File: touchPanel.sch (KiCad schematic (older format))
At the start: 54 parts, among them J19 Mono_AudioConnector, J20 Mono_AudioConnector, J21 Mono_AudioConnector, J22 Mono_AudioConnector

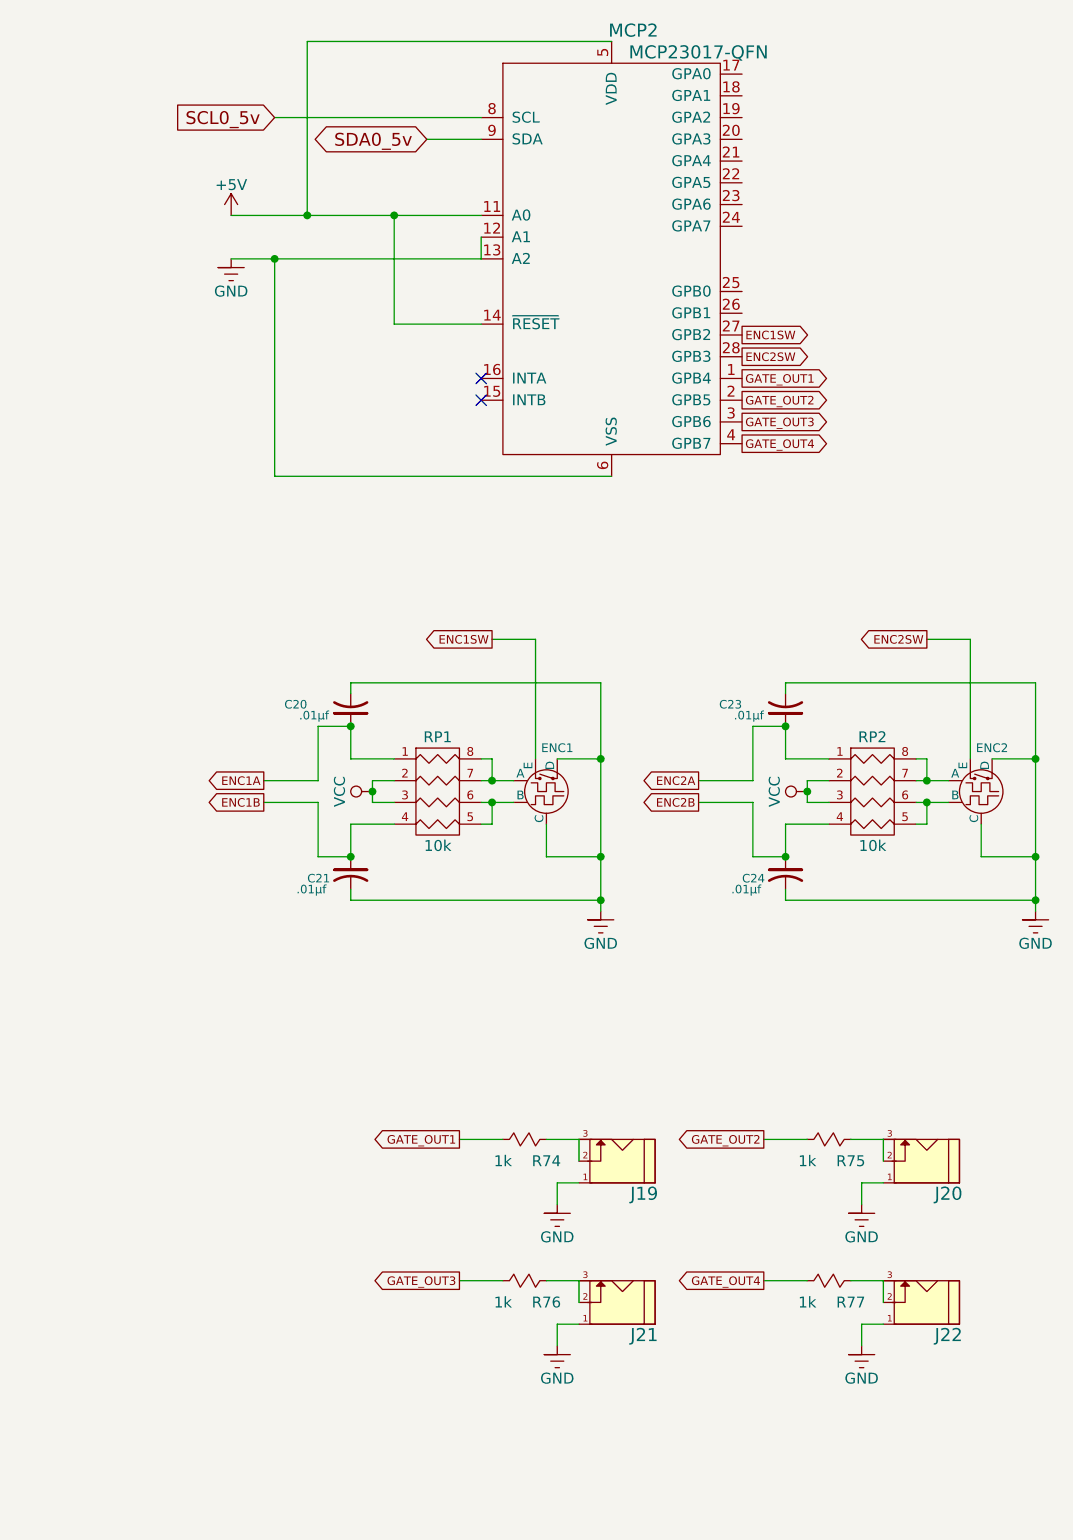
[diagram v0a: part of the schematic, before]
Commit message: Added Touch Capacitive Panel
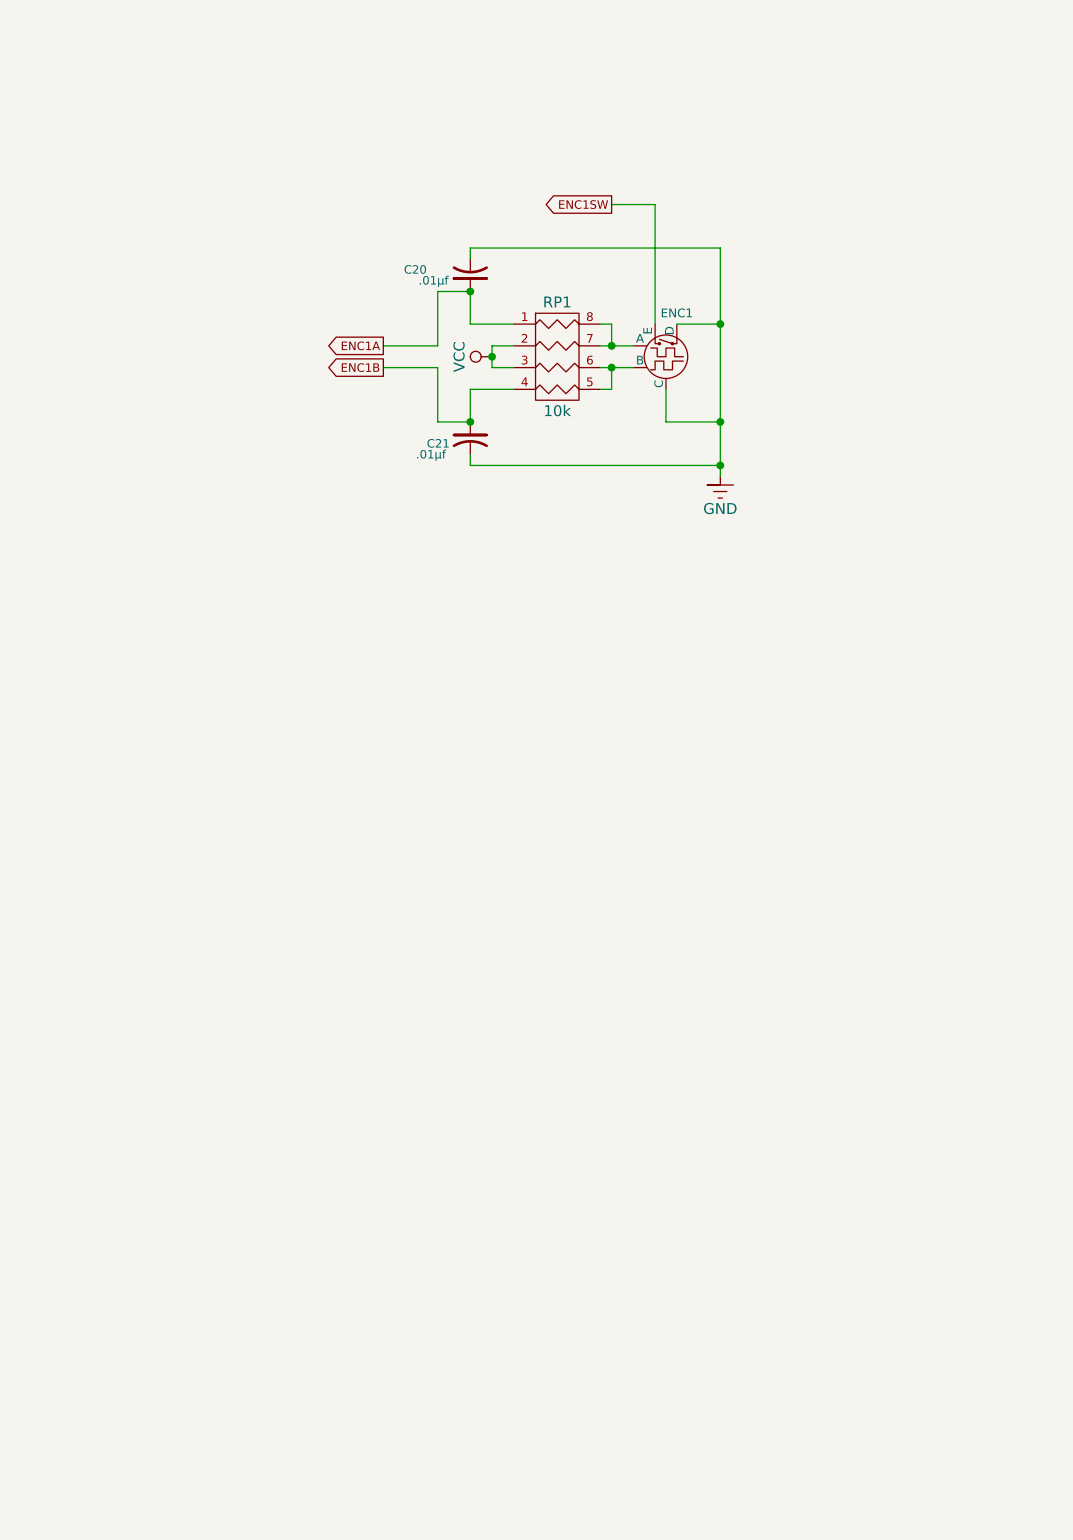
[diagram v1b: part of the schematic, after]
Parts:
- removed C23, C24: .01µf, Capacitors_SMD:C_0805_HandSoldering, symbol Cap
- removed ENC2: Encoder_switch, Zetaohm:AB2_ROTARY_ENCODER_W_SWITCH, symbol Encoder_switch
- removed J19, J20, J21, J22: Mono_AudioConnector, Zetaohm:THONKICONN, symbol Mono_AudioConnector
- removed MCP2: MCP23017-QFN, Housings_DFN_QFN:QFN-28-1EP_6x6mm_Pitch0.65mm, symbol MCP23017-QFN
- removed R74, R75, R76, R77: 1k, Resistors_SMD:R_0805_HandSoldering, symbol Resistor
- removed RP2: 10k, symbol R_PACK4
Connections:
- no-connect marks 2 -> 0
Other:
- moved on the sheet: C20, C21, ENC1, RP1

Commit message: Updating footprints
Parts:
- C20, C21: footprint Capacitors_SMD:C_0805_HandSoldering -> Capacitors_SMD:C_0603_HandSoldering
- C36, C41, C42, C43, C44, C45, C46, C47, C48, C49, C50, C51, C52: renamed from C?; footprint (none) -> Capacitors_SMD:C_0603_HandSoldering
- R15, R47, R48, R49, R50, R74, R75, R76, R77, R78, R79, R80, R81, R82, R83, R84, R85, R86, R87, R88: renamed from R?; footprint (none) -> Resistors_SMD:R_0603_HandSoldering
- RP1: footprint (none) -> Resistors_SMD:R_0603_HandSoldering
- U11: renamed from U?; footprint (none) -> Housings_SOT-23_SOT-143_TSOT-6:SOT-23_Handsoldering
- U12: renamed from U?; footprint (none) -> Housings_QFP:LQFP-44_10x10mm_Pitch0.8mm
- gave numbers to parts that had none: 2
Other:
- moved on the sheet: U14

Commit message: Populating pcb file
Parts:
- removed R48, R49, R50, R74, R75, R76, R77, R78, R79, R80, R81, R82: 1k, Resistors_SMD:R_0603_HandSoldering, symbol Resistor
- removed R85, R86, R87, R88: 470k, Resistors_SMD:R_0603_HandSoldering, symbol Resistor
- added RP2, RP3, RP4: 1k, Resistors_SMD:R_Array_Convex_4x0603, symbol R_PACK4
- added RP5: 470k, Resistors_SMD:R_Array_Convex_4x0603, symbol R_PACK4
- RP1: footprint Resistors_SMD:R_0603_HandSoldering -> Resistors_SMD:R_Array_Convex_4x0603
- U14: footprint (none) -> Zetaohm:FACEPLATEV1
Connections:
- net X0: now also RP2.8 (R1); no longer R15.1
- net X1: now also RP2.7 (R2); no longer R47.1
- net X2: now also RP2.6 (R3)
- net X3: now also RP2.5 (R4)
- net X4: now also RP3.8 (R1)
- net X5: now also RP3.7 (R2)
- net X6: now also RP3.6 (R3)
- net X7: now also RP3.5 (R4)
- net Y0: now also RP4.8 (R1)
- net Y1: now also RP4.7 (R2)
- net Y2: now also RP4.6 (R3)
- net Y3: now also RP4.5 (R4)
- net Y4: now also R15.1
- net Y5: now also R47.1
- net at R83.1, R84.1, U12.12 (SMP): now also RP5.5 (R4), RP5.6 (R3), RP5.7 (R2), RP5.8 (R1)
- net at C50.1, U12.13 (Y3A): now also RP4.4 (P4)
- net at C49.1, U12.14 (Y2A): now also RP4.3 (P3)
- net at C47.1, U12.15 (Y1A): now also RP4.2 (P2)
- net at C45.1, U12.16 (Y0A): now also RP4.1 (P1)
- net at U12.19 (X0): now also RP2.1 (P1); no longer R15.2
- net at U12.20 (X1): now also RP2.2 (P2); no longer R47.2
- net at U12.21 (X2): now also RP2.3 (P3)
- net at U12.22 (X3): now also RP2.4 (P4)
- net at U12.23 (X4): now also RP3.1 (P1)
- net at U12.24 (X5): now also RP3.2 (P2)
- net at U12.25 (X6): now also RP3.3 (P3)
- net at U12.26 (X7): now also RP3.4 (P4)
- net at C45.2, U12.30 (Y0B): now also RP5.1 (P1)
- net at C47.2, U12.31 (Y1B): now also RP5.2 (P2)
- net at C49.2, U12.32 (Y2B): now also RP5.3 (P3)
- net at C50.2, U12.33 (Y3B): now also RP5.4 (P4)
- net at C51.1, U12.34 (Y4A): now also R15.2
- net at U12.36 (Y5A): now also R47.2
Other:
- moved on the sheet: R83, R84

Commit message: UPDATING SCHEMATIC FOR SSD1327
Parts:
- U14: footprint Zetaohm:FACEPLATEV1 -> Zetaohm:AFX-01_FACEPLATE
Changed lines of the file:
@@
 $Descr User 15748 9843
 encoding utf-8
-Sheet 6 7
+Sheet 6 8
 Title ""
 Date ""
@@
 $EndComp
 $Comp
-L GND-RESCUE-afx-01 #PWR96
+L GND-RESCUE-afx-01 #PWR092
 U 1 1 56243B05
 P 13350 3150
-F 0 "#PWR96" H 13350 2900 50  0001 C CNN
+F 0 "#PWR092" H 13350 2900 50  0001 C CNN
 F 1 "GND" H 13350 3000 50  0000 C CNN
 F 2 "" H 13350 3150 60  0000 C CNN
@@
 $EndComp
 $Comp
-L VCC #PWR95
+L VCC #PWR093
 U 1 1 56243B1B
 P 12300 2600
-F 0 "#PWR95" H 12300 2450 50  0001 C CNN
+F 0 "#PWR093" H 12300 2450 50  0001 C CNN
 F 1 "VCC" H 12300 2750 50  0000 C CNN
 F 2 "" H 12300 2600 60  0000 C CNN
@@
 $EndComp
 $Comp
-L +5V #PWR92
+L +5V #PWR094
 U 1 1 56248DD8
 P 1950 1500
-F 0 "#PWR92" H 1950 1350 50  0001 C CNN
+F 0 "#PWR094" H 1950 1350 50  0001 C CNN
 F 1 "+5V" H 1950 1640 50  0000 C CNN
 F 2 "" H 1950 1500 60  0000 C CNN
@@
 F 0 "U14" H 12150 4200 60  0000 C CNN
 F 1 "AFX-01_BUTTON_MATRIX" H 12150 5200 60  0000 C CNN
-F 2 "Zetaohm:FACEPLATEV1" H 12150 4650 60  0001 C CNN
+F 2 "Zetaohm:AFX-01_FACEPLATE" H 12150 4650 60  0001 C CNN
 F 3 "" H 12150 4650 60  0000 C CNN
 	1    12150 4650
@@
 $EndComp
 $Comp
-L GND-RESCUE-afx-01 #PWR98
+L GND-RESCUE-afx-01 #PWR095
 U 1 1 56280C9D
 P 5100 5800
-F 0 "#PWR98" H 5100 5550 50  0001 C CNN
+F 0 "#PWR095" H 5100 5550 50  0001 C CNN
 F 1 "GND" H 5100 5650 50  0000 C CNN
 F 2 "" H 5100 5800 60  0000 C CNN
@@
 $EndComp
 $Comp
-L GND-RESCUE-afx-01 #PWR93
+L GND-RESCUE-afx-01 #PWR096
 U 1 1 5628B453
 P 5700 1550
-F 0 "#PWR93" H 5700 1300 50  0001 C CNN
+F 0 "#PWR096" H 5700 1300 50  0001 C CNN
 F 1 "GND" H 5700 1400 50  0000 C CNN
 F 2 "" H 5700 1550 60  0000 C CNN
@@
 Connection ~ 3100 1650
 $Comp
-L GND-RESCUE-afx-01 #PWR94
+L GND-RESCUE-afx-01 #PWR097
 U 1 1 5628D8FE
 P 2550 2400
-F 0 "#PWR94" H 2550 2150 50  0001 C CNN
+F 0 "#PWR097" H 2550 2150 50  0001 C CNN
 F 1 "GND" H 2550 2250 50  0000 C CNN
 F 2 "" H 2550 2400 60  0000 C CNN
@@
 Connection ~ 3900 4200
 $Comp
-L GND-RESCUE-afx-01 #PWR97
+L GND-RESCUE-afx-01 #PWR098
 U 1 1 562924E5
 P 2650 4400
-F 0 "#PWR97" H 2650 4150 50  0001 C CNN
+F 0 "#PWR098" H 2650 4150 50  0001 C CNN
 F 1 "GND" H 2650 4250 50  0000 C CNN
 F 2 "" H 2650 4400 60  0000 C CNN
